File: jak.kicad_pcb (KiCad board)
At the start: 2 copper layers, 230.7 x 96.9 mm, 94 parts, among them SW1 SW_Push, SW10 SW_Push, SW10_r1 SW_Push, SW11 SW_Push, SW11_r1 SW_Push, SW12 SW_Push, SW12_r1 SW_Push, SW13 SW_Push, SW13_r1 SW_Push, SW14 SW_Push, SW14_r1 SW_Push, SW15 SW_Push, SW15_r1 SW_Push, SW16 SW_Push, SW16_r1 SW_Push, SW17 SW_Push, SW17_r1 SW_Push, SW18 SW_Push, SW18_r1 SW_Push, SW1_r1 SW_Push, SW2 SW_Push, SW2_r1 SW_Push, SW3 SW_Push, SW3_r1 SW_Push, SW4 SW_Push, SW4_r1 SW_Push, SW5 SW_Push, SW5_r1 SW_Push, SW6 SW_Push, SW6_r1 SW_Push, SW7 SW_Push, SW7_r1 SW_Push, SW8 SW_Push, SW8_r1 SW_Push, SW9 SW_Push, SW9_r1 SW_Push

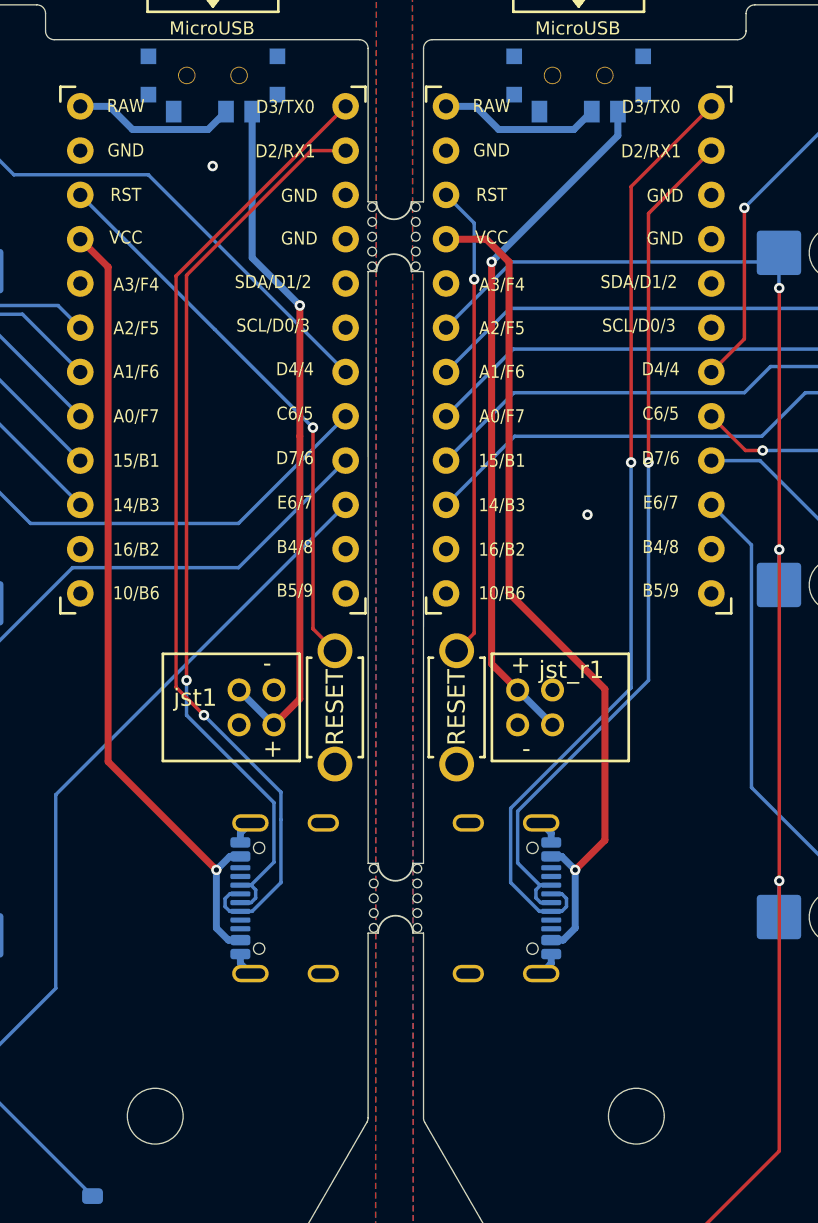
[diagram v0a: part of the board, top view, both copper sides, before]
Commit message: Replaced the through-hole surface USB-C connector with a flush one
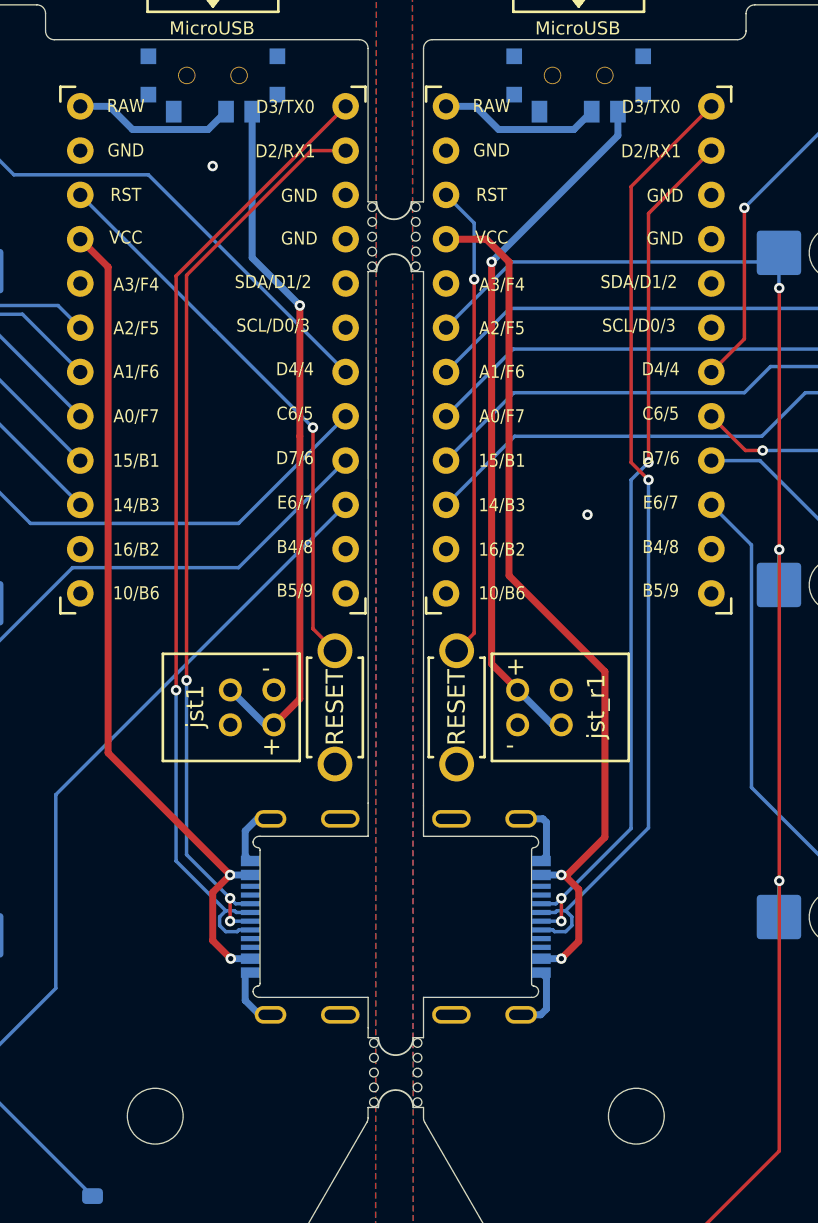
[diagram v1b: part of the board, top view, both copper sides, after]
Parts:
- controller_r1: value ProMicro_r -> ProMicro
- split_connector1, split_connector_r1: footprint Connector_USB:USB_C_Receptacle_GCT_USB4105-xx-A_16P_TopMnt_Horizontal -> USB4505-03-0-A_REVA:GCT_USB4505-03-0-A_REVA
- moved REF** 10.0 mm to (147.5, 121.5)
- moved split_connector1 2.31 mm to (143.3, 112.6)
- moved split_connector_r1 2.31 mm to (149.7, 112.6)
- moved jst2 0.50 mm to (137.0, 101.6)
- moved jst_r2 0.50 mm to (156.0, 99.6)
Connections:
- split_connector1 pad A8: (no net) -> unconnected-(split_connector1-SBU1-PadA8)
- split_connector1 pad B8: (no net) -> unconnected-(split_connector1-SBU2-PadB8)
- split_connector_r1 pad A8: (no net) -> unconnected-(split_connector_r1-SBU1-PadA8)
- split_connector_r1 pad B8: (no net) -> unconnected-(split_connector_r1-SBU2-PadB8)
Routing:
- net GND_r: track 2.72 -> 7.69 mm, vias 1 -> 0
- net GND: track 2.72 -> 6.68 mm
- net VCC_r: track 48.7 -> 50.9 mm, vias 1 -> 2
- net VCC: track 46.1 -> 48.0 mm, vias 1 -> 2
- net split_comms+: track 56.5 -> 55.8 mm
- net split_comms-: track 52.1 -> 52.6 mm, vias 1 -> 3
- net split_comms+_r: track 49.7 -> 50.2 mm, vias 1 -> 3
- net (no net): vias 0 -> 1
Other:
- outline, holes or cut-outs redrawn
